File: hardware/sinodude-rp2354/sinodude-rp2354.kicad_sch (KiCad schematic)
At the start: 93 parts, among them J1 USB-C, J2 SWD TC2030-IDC latching, J4 DUT, Q1 2N7002, SW1 BOOTSEL, SW2 RESET, U1 RP2354A, U2 AMS1117-3.3, U3 TPS2114APW, U4 SN74LVC8T245PW, U5 SN74LVC1T45DBV, U6 SN74LVC1T45DBV, Y1 12MHz/CL10pF/ESR50R/ABM8-272-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

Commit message: hardware: M3 mounting holes, U1 decoupling back to top side
Mounting holes go M2.5 -> M3 (3.2 mm drill), inset to clear U2 and J4.

Move U1's decoupling back to the top, ringed around the package. Building the
net map showed why the bottom-side version could not work: the QFN's pad rows
sit directly above the bottom cap pads, so a via at a cap would land under
pins 25/26 (SWDIO/RUN). QFN-60 is peripheral-only, so a top-side ring reaches
every rail pin with a direct trace and no via in the decoupling loop at all.

Pull-ups, LED and CC resistors, and the non-U1 bypass caps stay on the bottom.

Also nudged for routing: R6 beside the crystal instead of 9 mm from XOUT, R7
between U1 and SW1, R1/R2 against J1's CC pads, the VTGT sense divider onto
the VTGT cluster, and R19/R20 next to Q1's gate.
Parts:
- H1, H2, H3, H4: value MountingHole -> MountingHole M3; footprint MountingHole:MountingHole_2.7mm_M2.5 -> MountingHole:MountingHole_3.2mm_M3
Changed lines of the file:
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@@
 			)
 		)
-		(property "Value" "MountingHole"
+		(property "Value" "MountingHole M3"
 			(at 375.92 321.945 0)
 			(show_name no)
@@
 			)
 		)
-		(property "Footprint" "MountingHole:MountingHole_2.7mm_M2.5"
+		(property "Footprint" "MountingHole:MountingHole_3.2mm_M3"
 			(at 375.92 325.12 0)
 			(hide yes)
@@
 			)
 		)
-		(property "Value" "MountingHole"
+		(property "Value" "MountingHole M3"
 			(at 444.5 321.945 0)
 			(show_name no)
@@
 			)
 		)
-		(property "Footprint" "MountingHole:MountingHole_2.7mm_M2.5"
+		(property "Footprint" "MountingHole:MountingHole_3.2mm_M3"
 			(at 444.5 325.12 0)
 			(hide yes)
@@
 			)
 		)
-		(property "Value" "MountingHole"
+		(property "Value" "MountingHole M3"
 			(at 421.64 321.945 0)
 			(show_name no)
@@
 			)
 		)
-		(property "Footprint" "MountingHole:MountingHole_2.7mm_M2.5"
+		(property "Footprint" "MountingHole:MountingHole_3.2mm_M3"
 			(at 421.64 325.12 0)
 			(hide yes)
@@
 			)
 		)
-		(property "Value" "MountingHole"
+		(property "Value" "MountingHole M3"
 			(at 398.78 321.945 0)
 			(show_name no)
@@
 			)
 		)
-		(property "Footprint" "MountingHole:MountingHole_2.7mm_M2.5"
+		(property "Footprint" "MountingHole:MountingHole_3.2mm_M3"
 			(at 398.78 325.12 0)
 			(hide yes)

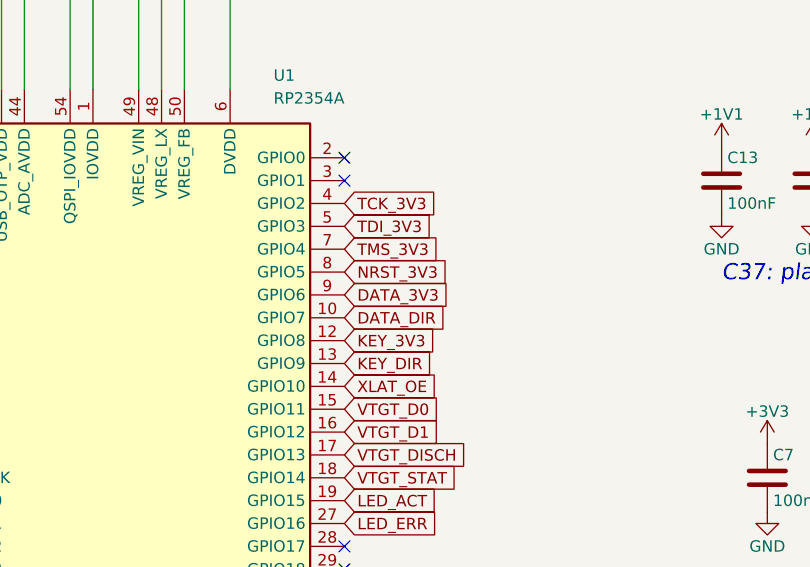
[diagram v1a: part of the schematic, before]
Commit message: hardware: route the RP2354 board on a 68x36 mm two-layer outline
Shrinks the outline from 75x40 mm and re-floorplans into blocks: USB and the
3V3 regulator west, SWD and clock north, target supply and level shifters east,
discharge south-east, both buttons together under U4. M3 mounting holes.

Reassigns U1's GPIOs so the JTAG group and DATA/KEY leave the east column in the
order U4, U5/U6 and the DUT header need them. Assigned the other way round they
have to cross inside the 0.4 mm pad ring, where there is no room.

Design rules drop to 0.15 mm track and clearance with board minimums set to
JLCPCB's two-layer capability, which is what makes the QFN escapes fit. Ground
pours use solid pad connections, since thermal spokes starve on two layers, and
are stitched together.

The Tag-Connect, the USB pair and the VBUS bridge are routed by hand: J2's leg
holes leave one single-track channel per pad and which channel a pad may use is
forced by geometry, so no autorouter finds them.

DRC is clean. Two connections remain open, KEY_DIR and U1's ground pin 47, both
noted in the README.
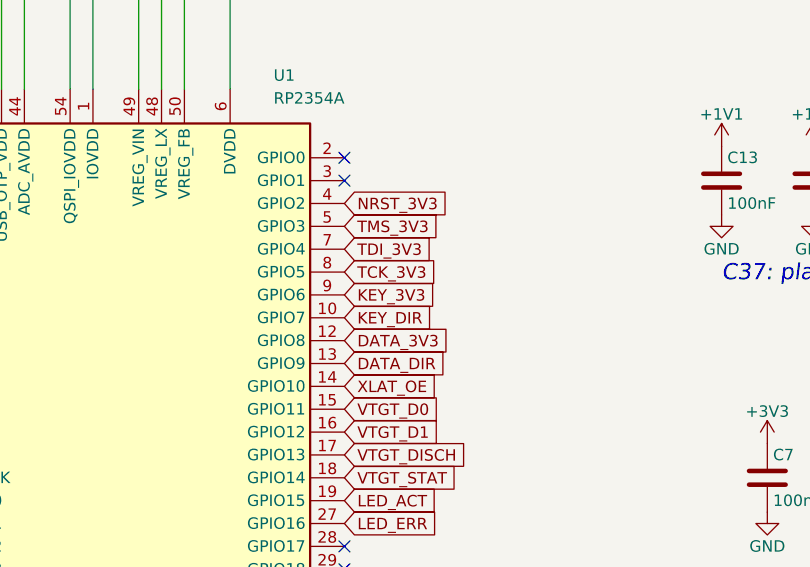
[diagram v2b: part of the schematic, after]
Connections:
- net DATA_3V3: now also U1.12 (GPIO8); no longer U1.9 (GPIO6)
- net DATA_DIR: now also U1.13 (GPIO9); no longer U1.10 (GPIO7)
- net KEY_3V3: now also U1.9 (GPIO6); no longer U1.12 (GPIO8)
- net KEY_DIR: now also U1.10 (GPIO7); no longer U1.13 (GPIO9)
- net NRST_3V3: now also U1.4 (GPIO2); no longer U1.8 (GPIO5)
- net TCK_3V3: now also U1.8 (GPIO5); no longer U1.4 (GPIO2)
- net TDI_3V3: now also U1.7 (GPIO4); no longer U1.5 (GPIO3)
- net TMS_3V3: now also U1.5 (GPIO3); no longer U1.7 (GPIO4)
